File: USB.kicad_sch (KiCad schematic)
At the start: 35 parts, among them J1 USB_C_Receptable_USB2.0, U1 AP2141WG-7, U2 3V3

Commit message: Apply JLCPCB rotations and offsets to components
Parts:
- J1: JLCPCB Position Offset (none) -> 0,1.26
- U1: JLCPCB Rotation Offset (none) -> 180
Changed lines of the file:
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@@
 	(title_block
 		(title "Tiny Scarab")
-		(date "2024-01-30")
+		(date "2024-03-04")
 		(rev "0.2")
 		(company "Embeetle")
@@
 			)
 		)
-		(property "Description" ""
+		(property "Description" "Unpolarized capacitor"
 			(at 73.66 55.88 0)
 			(effects
@@
 			)
 		)
-		(property "Description" ""
+		(property "Description" "Power symbol creates a global label with name \"GND\" , ground"
 			(at 25.4 87.63 0)
 			(effects
@@
 			)
 		)
-		(property "Description" ""
+		(property "Description" "Schottky diode 40V 350mA"
 			(at 119.38 73.66 0)
 			(effects
@@
 			)
 		)
-		(property "Description" ""
+		(property "Description" "TVS diode bidirectional 5V, 1pF"
 			(at 48.26 72.39 0)
 			(effects
@@
 			)
 		)
-		(property "Description" ""
+		(property "Description" "Unpolarized capacitor"
 			(at 67.31 55.88 0)
 			(effects
@@
 			)
 		)
-		(property "Description" ""
+		(property "Description" "Power symbol creates a global label with name \"GND\" , ground"
 			(at 86.36 62.23 0)
 			(effects
@@
 			)
 		)
-		(property "Description" ""
+		(property "Description" "Power symbol creates a global label with name \"+5V\""
 			(at 191.77 33.02 0)
 			(effects
@@
 			)
 		)
-		(property "Description" ""
+		(property "Description" "Resistor"
 			(at 191.77 39.37 0)
 			(effects
@@
 			)
 		)
-		(property "Description" ""
+		(property "Description" "Power symbol creates a global label with name \"GND\" , ground"
 			(at 170.18 96.52 0)
 			(effects
@@
 			)
 		)
-		(property "Description" ""
+		(property "Description" "Unpolarized capacitor"
 			(at 30.48 118.11 0)
 			(effects
@@
 			)
 		)
-		(property "Description" ""
+		(property "Description" "Unpolarized capacitor"
 			(at 43.18 118.11 0)
 			(effects
@@
 			)
 		)
-		(property "Description" ""
+		(property "Description" "Power symbol creates a global label with name \"+5V\""
 			(at 99.06 80.01 0)
 			(effects
@@
 			)
 		)
-		(property "Description" ""
+		(property "Description" "Unpolarized capacitor"
 			(at 49.53 118.11 0)
 			(effects
@@
 			)
 		)
-		(property "Description" ""
+		(property "Description" "Power symbol creates a global label with name \"GND\" , ground"
 			(at 120.65 62.23 0)
 			(effects
@@
 			)
 		)
-		(property "Description" ""
+		(property "Description" "Unpolarized capacitor"
 			(at 105.41 55.88 0)
 			(effects
@@
 			)
 		)
-		(property "Description" ""
+		(property "Description" "Unpolarized capacitor"
 			(at 80.01 91.44 0)
 			(effects
@@
 			)
 		)
-		(property "Description" ""
+		(property "Description" "Unpolarized capacitor"
 			(at 36.83 118.11 0)
 			(effects
@@
 			)
 		)
-		(property "Description" ""
+		(property "Description" "Power symbol creates a global label with name \"GND\" , ground"
 			(at 24.13 125.73 0)
 			(effects
@@
 			)
 		)
-		(property "Description" ""
+		(property "Description" "Power symbol creates a global label with name \"+5V\""
 			(at 171.45 90.17 0)
 			(effects
@@
 			)
 		)
-		(property "Description" ""
+		(property "Description" "Unpolarized capacitor"
 			(at 86.36 91.44 0)
 			(effects
@@
 			)
 		)
-		(property "Description" ""
+		(property "Description" "Unpolarized capacitor"
 			(at 99.06 91.44 0)
 			(effects
@@
 			)
 		)
-		(property "Description" ""
+		(property "Description" "Unpolarized capacitor"
 			(at 92.71 91.44 0)
 			(effects
@@
 			)
 		)
-		(property "Description" ""
+		(property "Description" "Resistor"
 			(at 147.32 45.72 0)
 			(effects
@@
 			)
 		)
-		(property "Description" ""
+		(property "Description" "Unpolarized capacitor"
 			(at 144.78 91.44 0)
 			(effects
@@
 			)
 		)
-		(property "Description" ""
+		(property "Description" "Power symbol creates a global label with name \"+3V3\""
 			(at 171.45 92.71 0)
 			(effects
@@
 			)
 		)
-		(property "Description" ""
+		(property "Description" "Resistor"
 			(at 175.26 58.42 0)
 			(effects
@@
 			)
 		)
-		(property "Description" ""
+		(property "Description" "Unpolarized capacitor"
 			(at 105.41 91.44 0)
 			(effects
@@
 			)
 		)
-		(property "Description" ""
+		(property "Description" "USB 2.0-only type-C receptable connector"
 			(at 25.4 62.23 0)
 			(effects
@@
 			)
 		)
+		(property "JLCPCB Position Offset" "0,1.26"
+			(at 25.4 62.23 0)
+			(effects
+				(font
+					(size 1.27 1.27)
+				)
+				(hide yes)
+			)
+		)
 		(pin "B8"
 		)
@@
 			)
 		)
-		(property "Description" ""
+		(property "Description" "Resistor"
 			(at 142.24 45.72 0)
 			(effects
@@
 			)
 		)
-		(property "Description" ""
+		(property "Description" "Power symbol creates a global label with name \"+3V3\""
 			(at 138.43 80.01 0)
 			(effects
@@
 			)
 		)
-		(property "Description" ""
+		(property "Description" "Unpolarized capacitor"
 			(at 55.88 118.11 0)
 			(effects
@@
 			)
 		)
-		(property "Description" ""
+		(property "Description" "Power symbol creates a global label with name \"GND\" , ground"
 			(at 186.69 62.23 0)
 			(effects
@@
 			)
 		)
-		(property "Description" ""
+		(property "Description" "Power symbol creates a global label with name \"+5V\""
 			(at 24.13 110.49 0)
 			(effects
@@
 			)
 		)
-		(property "Description" ""
+		(property "Description" "Unpolarized capacitor"
 			(at 138.43 91.44 0)
 			(effects
@@
 			)
 		)
-		(property "Description" ""
+		(property "Description" "Fuse 2A, 32V, 57mΩ, fast blow"
 			(at 86.36 49.53 0)
 			(effects
@@
 			)
 		)
-		(property "Description" ""
+		(property "Description" "Unpolarized capacitor"
 			(at 99.06 55.88 0)
 			(effects
@@
 			)
 		)
-		(property "Description" ""
+		(property "Description" "Unpolarized capacitor"
 			(at 24.13 118.11 0)
 			(effects
@@
 			)
 		)
-		(property "Description" ""
+		(property "Description" "Zener diode 5V6 (5V32-5V92) 1W"
 			(at 92.71 55.88 0)
 			(effects
@@
 			)
 		)
-		(property "Description" ""
+		(property "Description" "Power symbol creates a global label with name \"GND\" , ground"
 			(at 50.8 81.28 0)
 			(effects
@@
 			)
 		)
-		(property "Description" ""
+		(property "Description" "LED green 0603"
 			(at 186.69 50.8 0)
 			(effects
@@
 			)
 		)
-		(property "Description" ""
+		(property "Description" "Current limited power switch, single channel"
 			(at 120.65 52.07 0)
 			(effects
@@
 			)
 		)
+		(property "JLCPCB Rotation Offset" "180"
+			(at 120.65 52.07 0)
+			(effects
+				(font
+					(size 1.27 1.27)
+				)
+				(hide yes)
+			)
+		)
 		(pin "2"
 		)
@@
 			)
 		)
-		(property "Description" ""
+		(property "Description" "TVS unidirectional, 400W, 5V"
 			(at 80.01 55.88 0)
 			(effects
@@
 			)
 		)
-		(property "Description" ""
+		(property "Description" "TVS diode bidirectional 5V, 1pF"
 			(at 53.34 72.39 0)
 			(effects
@@
 			)
 		)
-		(property "Description" ""
+		(property "Description" "Power symbol creates a global label with name \"+5V\""
 			(at 134.62 48.26 0)
 			(effects
@@
 			)
 		)
-		(property "Description" ""
+		(property "Description" "Unpolarized capacitor"
 			(at 17.78 118.11 0)
 			(effects
@@
 			)
 		)
-		(property "Description" ""
+		(property "Description" "Resistor"
 			(at 175.26 55.88 0)
 			(effects
@@
 			)
 		)
-		(property "Description" ""
+		(property "Description" "Unpolarized capacitor"
 			(at 132.08 91.44 0)
 			(effects
@@
 			)
 		)
-		(property "Description" ""
+		(property "Description" "Power symbol creates a global label with name \"GND\" , ground"
 			(at 119.38 99.06 0)
 			(effects
@@
 			)
 		)
-		(property "Description" ""
+		(property "Description" "LED red 0603"
 			(at 138.43 54.61 0)
 			(effects
@@
 			)
 		)
-		(property "Description" ""
+		(property "Description" "LDO (Low-dropout) linear voltage regulator 3V3, 500mA"
 			(at 119.38 85.09 0)
 			(effects

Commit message: My hands are typing words
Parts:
- J1: JLCPCB Position Offset 0,1.26 -> 0,1.22
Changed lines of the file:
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@@
 			)
 		)
-		(property "JLCPCB Position Offset" "0,1.26"
+		(property "JLCPCB Position Offset" "0,1.22"
 			(at 25.4 62.23 0)
 			(effects

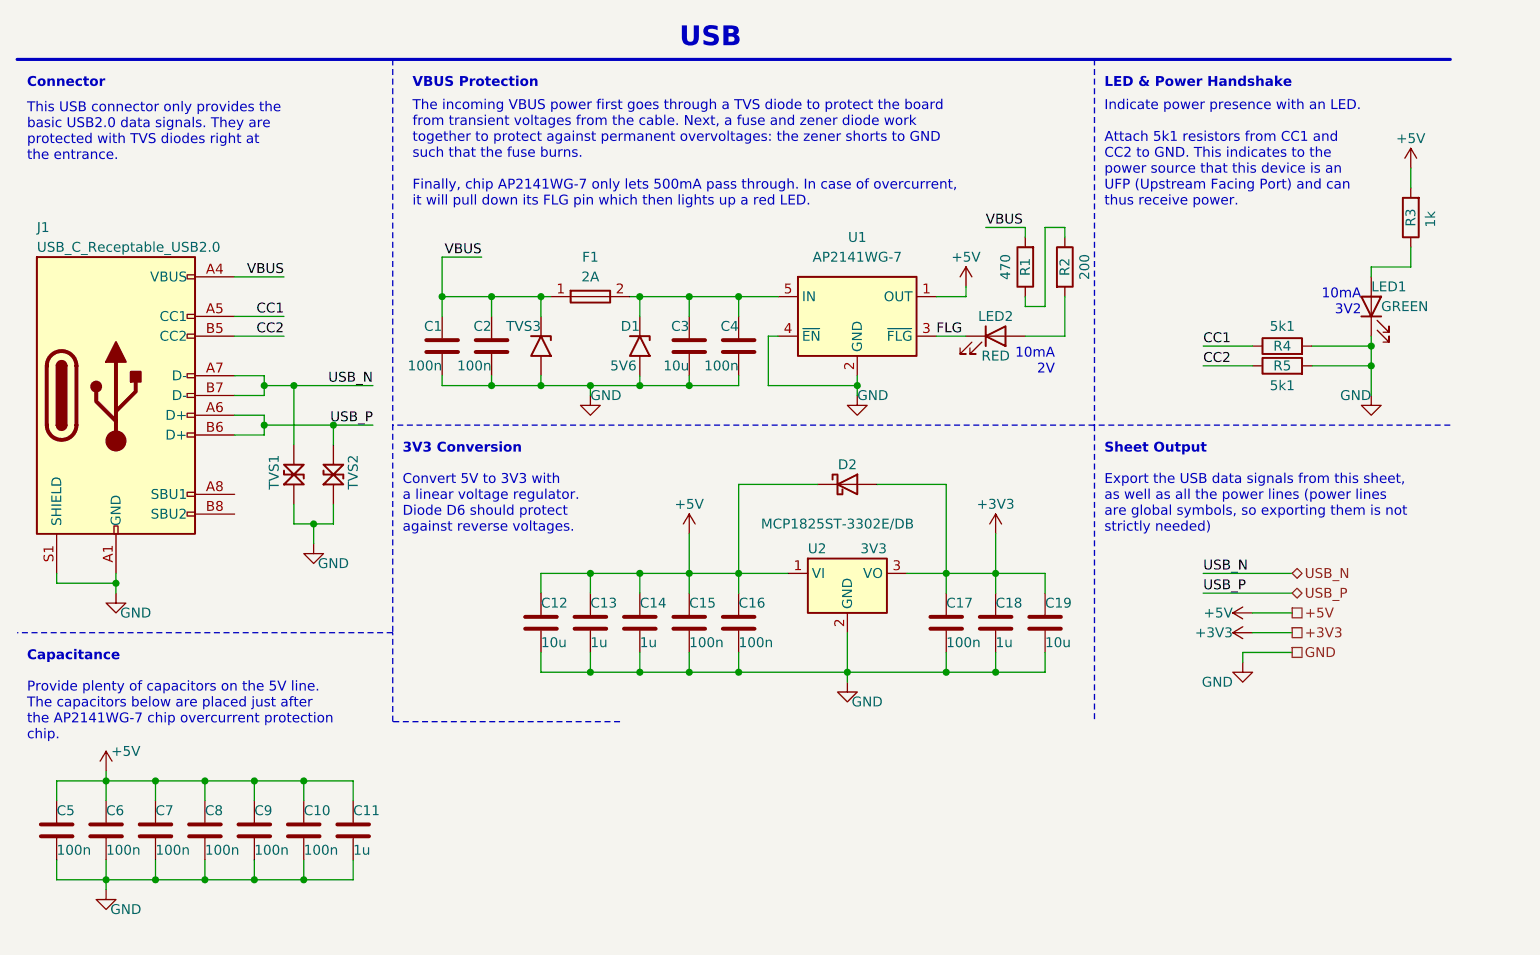
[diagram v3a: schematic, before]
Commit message: Insert green and red LED
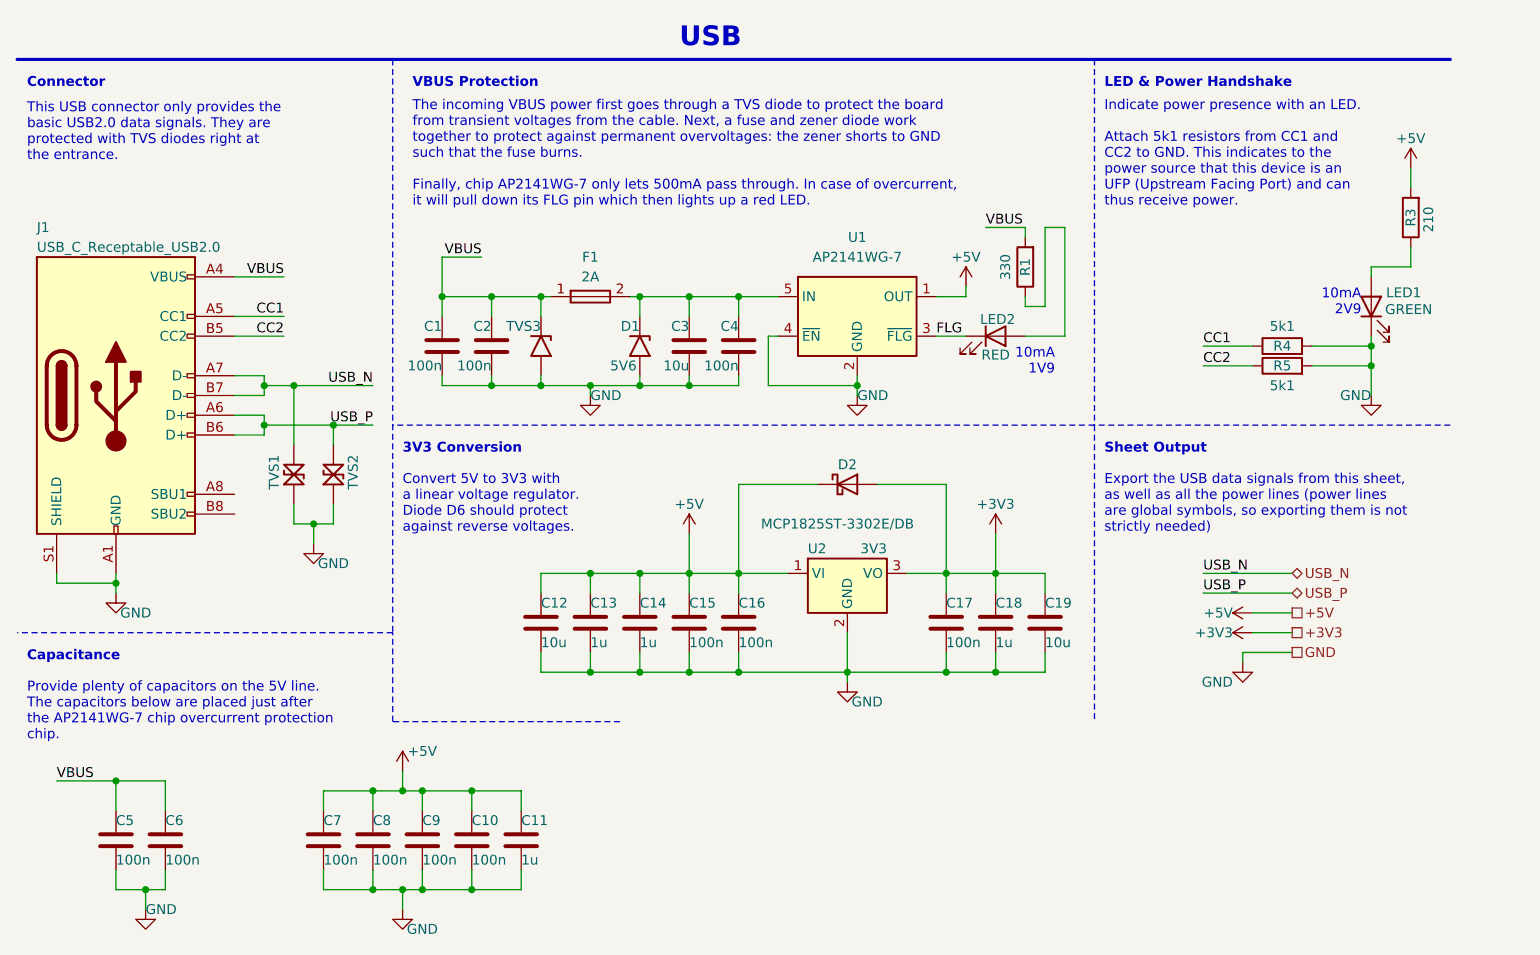
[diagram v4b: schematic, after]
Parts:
- removed LED1: GREEN, Tiny_Scarab:LED_0603_CSL0902ET, symbol Tiny_Scarab:LED_GREEN_CSL0902ET
- removed LED2: RED, Tiny_Scarab:LED_0603_CSL0902UT, symbol Tiny_Scarab:LED_RED_CSL0902UT
- removed R2: 200, Resistor_SMD:R_0402_1005Metric_Pad0.72x0.64mm_HandSolder, symbol Device:R
- added LED1: GREEN, Tiny_Scarab:LED_D3.0mm_green, symbol Tiny_Scarab:LED_GREEN_XSW24061001
- added LED2: RED, Tiny_Scarab:LED_D3.0mm_red, symbol Tiny_Scarab:LED_RED_XSW24061002
- R1: value 470 -> 330; JLCPCB Part # C25117 -> C25104; MPN 0402WGF4700TCE -> 0402WGF3300TCE
- R3: value 1k -> 210; JLCPCB Part # C11702 -> C25090; MPN 0402WGF1001TCE -> 0402WGF2100TCE
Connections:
- net +5V: no longer C5.1, C6.1
- net FLG: now also LED2.1 (K)
- net GND: now also LED1.1 (K)
- net VBUS: now also C5.1, C6.1
- net at R3.1: now also LED1.2 (A)
- net at R1.1: now also LED2.2 (A)
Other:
- note added: "10mA 1V9"
- note added: "10mA 2V9"
- note removed: "10mA 2V"
- note removed: "10mA 3V2"
- moved on the sheet: C10, C11, C5, C6, C7, C8, C9

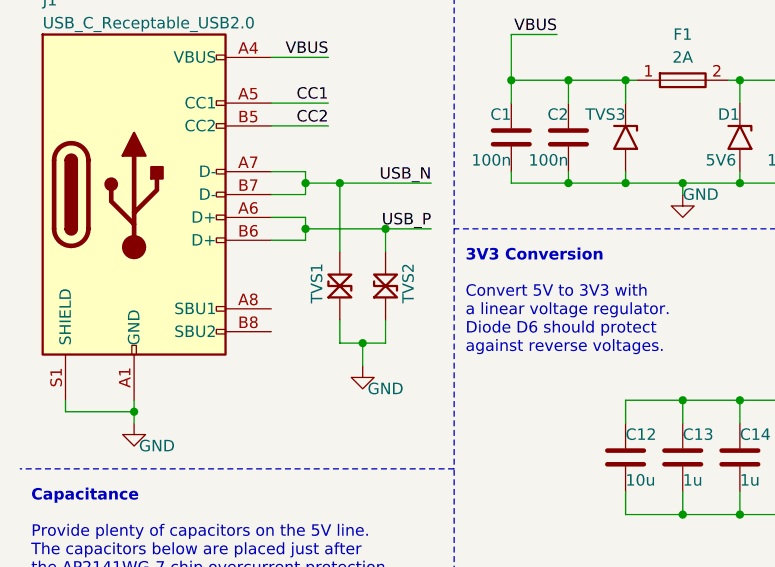
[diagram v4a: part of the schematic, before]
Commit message: Replace TVS `CDSOD323-T05LC` with `RLSD32A051LC`
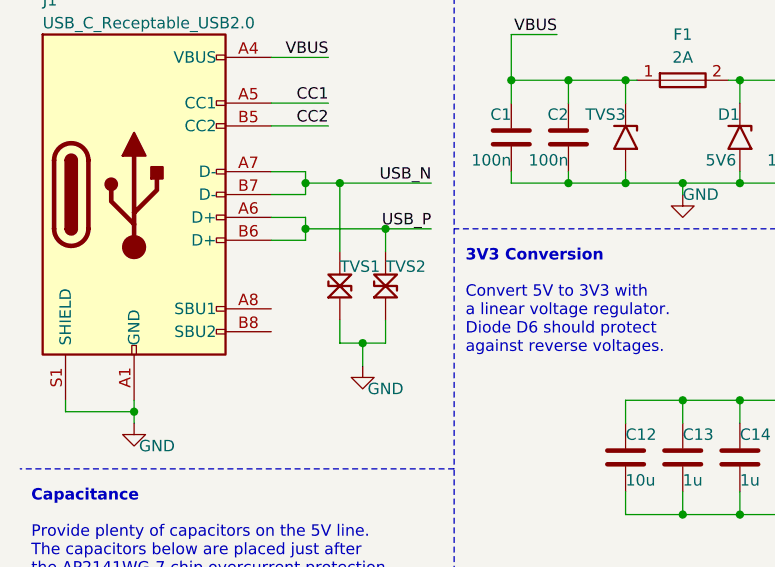
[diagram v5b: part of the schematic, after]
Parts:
- removed TVS1, TVS2: 5V, Tiny_Scarab:D_SOD-323_CDSOD323-T05LC, symbol Tiny_Scarab:TVS_CDSOD323-T05LC
- added TVS1, TVS2: 5V, Tiny_Scarab:D_SOD-323_CDSOD323-T05LC, symbol Tiny_Scarab:TVS_RLSD32A051LC
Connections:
- net GND: now also TVS1.2, TVS2.2
- net USB_N: now also TVS1.1
- net USB_P: now also TVS2.1
